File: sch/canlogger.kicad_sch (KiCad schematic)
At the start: 0 parts

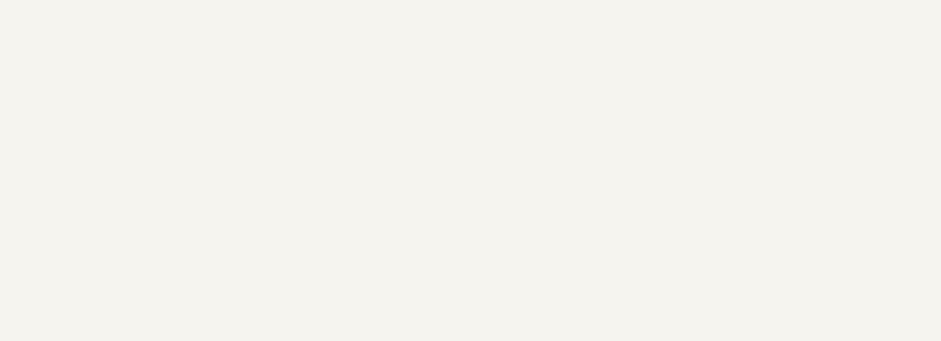
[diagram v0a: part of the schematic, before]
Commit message: v1.1 changes * increase LED resistors as they are too bright * replace solder jumpers with pins * add corresponding 3D models
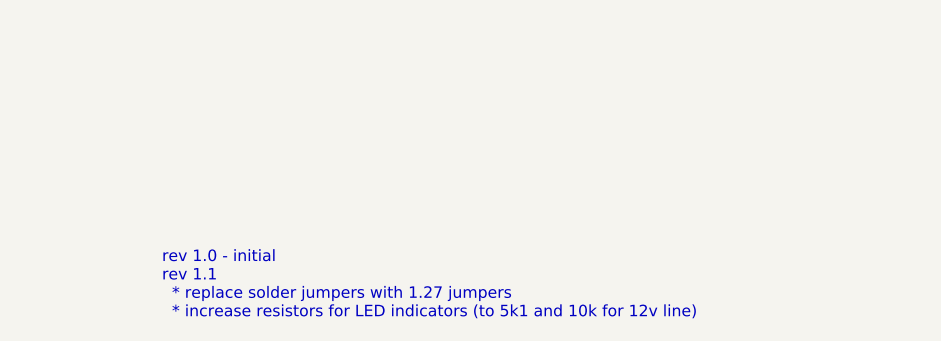
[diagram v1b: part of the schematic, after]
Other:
- note added: "rev 1.0 - initial rev 1.1 * replace solder jumpers with 1.27 jumpers * increase resistors for LED indicators (to 5k1 and 10k for 12v line)"
- title: 2CH CAN  Logger -> Dual Channel CAN Logger
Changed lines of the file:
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@@
 	(paper "A4")
 	(title_block
-		(title "2CH CAN  Logger")
-		(rev "1.0")
+		(title "Dual Channel CAN Logger")
+		(rev "1.1")
+	)
+	(text "rev 1.0 - initial\nrev 1.1 \n  * replace solder jumpers with 1.27 jumpers\n  * increase resistors for LED indicators (to 5k1 and 10k for 12v line)"
+		(exclude_from_sim no)
+		(at 182.372 153.416 0)
+		(effects
+			(font
+				(size 1.27 1.27)
+			)
+			(justify left)
+		)
 	)
 	(sheet
